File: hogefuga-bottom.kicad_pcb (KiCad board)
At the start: 2 copper layers, 95.2 x 97.6 mm, 6 parts

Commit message: rev0.2
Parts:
- removed the REF** at (90.5, 126.2)
- removed the REF** at (147.6, 88.1)
- removed the REF** at (90.5, 88.1)
- removed the REF** at (147.6, 126.2)
- added REF**: MountingHole_2.2mm_M2, MountingHole:MountingHole_2.2mm_M2, F.Cu at (131.0, 78.6)
- added REF**: MountingHole_2.2mm_M2, MountingHole:MountingHole_2.2mm_M2, F.Cu at (131.0, 116.7)
- added REF**: MountingHole_2.2mm_M2, MountingHole:MountingHole_2.2mm_M2, F.Cu at (73.8, 116.7)
- added REF**: MountingHole_2.2mm_M2, MountingHole:MountingHole_2.2mm_M2, F.Cu at (73.8, 78.6)
- moved G*** 19.2 mm to (102.4, 100.0) (x2)
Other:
- board size 95.2 x 97.6 mm -> 95.3 x 97.6 mm

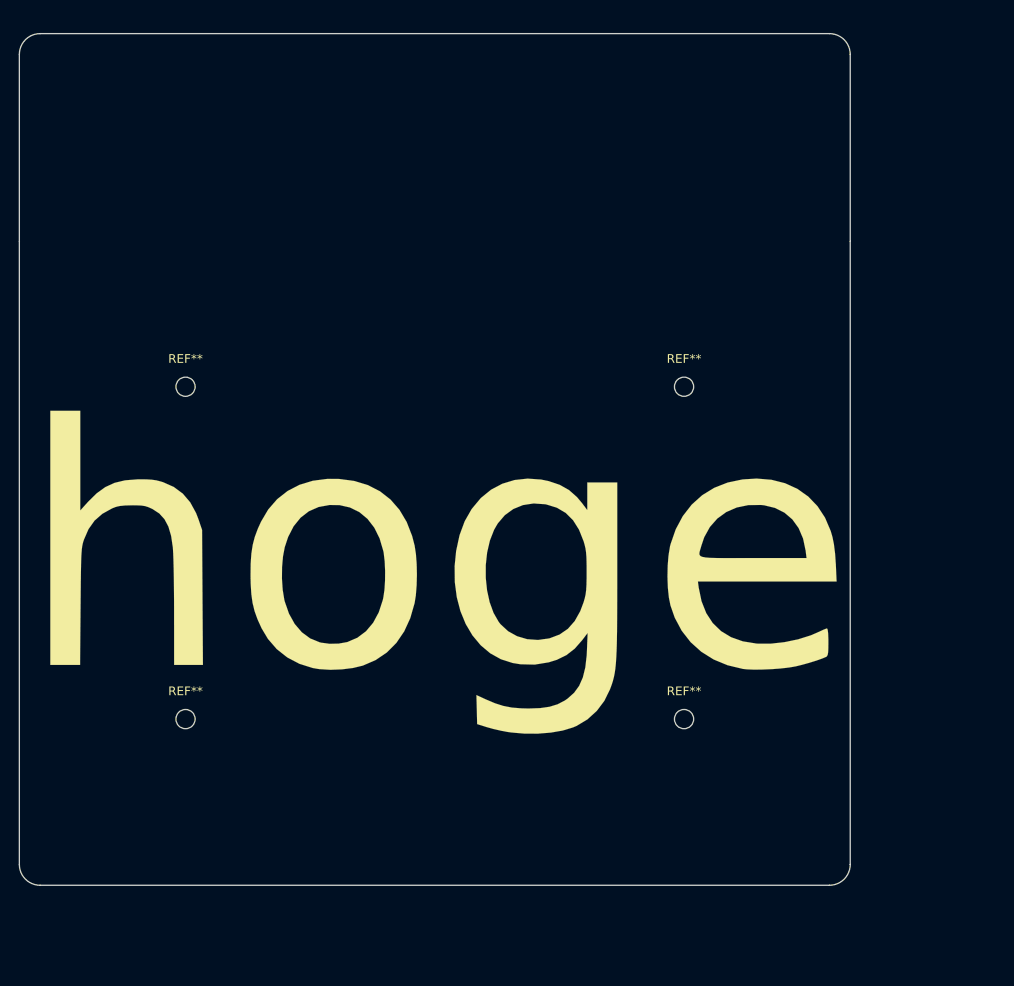
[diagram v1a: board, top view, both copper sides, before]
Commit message: PCBを直接ボトムプレートに固定する穴を追加
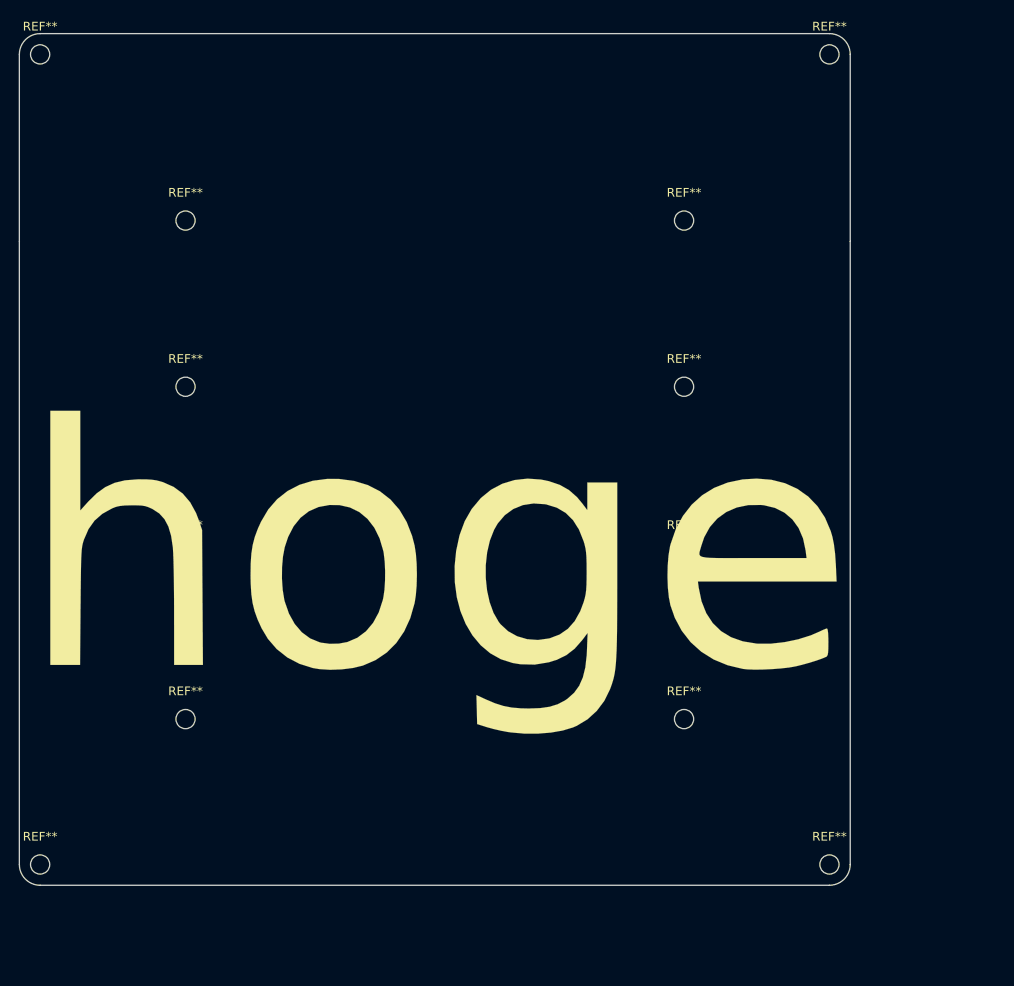
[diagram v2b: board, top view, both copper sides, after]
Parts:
- added REF**: MountingHole_2.2mm_M2, MountingHole:MountingHole_2.2mm_M2, F.Cu at (73.8, 97.6)
- added REF**: MountingHole_2.2mm_M2, MountingHole:MountingHole_2.2mm_M2, F.Cu at (73.8, 59.5)
- added REF**: MountingHole_2.2mm_M2, MountingHole:MountingHole_2.2mm_M2, F.Cu at (131.0, 59.5)
- added REF**: MountingHole_2.2mm_M2, MountingHole:MountingHole_2.2mm_M2, F.Cu at (147.6, 40.5)
- added REF**: MountingHole_2.2mm_M2, MountingHole:MountingHole_2.2mm_M2, F.Cu at (57.1, 40.5)
- added REF**: MountingHole_2.2mm_M2, MountingHole:MountingHole_2.2mm_M2, F.Cu at (57.1, 133.3)
- added REF**: MountingHole_2.2mm_M2, MountingHole:MountingHole_2.2mm_M2, F.Cu at (147.6, 133.3)
- added REF**: MountingHole_2.2mm_M2, MountingHole:MountingHole_2.2mm_M2, F.Cu at (131.0, 97.6)
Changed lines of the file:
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@@
     (tracks 0)
     (zones 0)
-    (modules 6)
+    (modules 14)
     (nets 1)
   )
@@
     (34 B.Paste user)
     (35 F.Paste user)
-    (36 B.SilkS user)
-    (37 F.SilkS user)
+    (36 B.SilkS user hide)
+    (37 F.SilkS user hide)
     (38 B.Mask user)
     (39 F.Mask user)
@@
       (xy 4.326291 11.84335) (xy 5.83656 12.123249) (xy 7.203423 12.18999) (xy 8.924412 12.091771)) (layer B.SilkS) (width 0.01))
   )
+  (module MountingHole:MountingHole_2.2mm_M2 (layer F.Cu)
+    (at 147.6375 40.48125)
+    (descr "Mounting Hole 2.2mm, no annular, M2")
+    (tags "mounting hole 2.2mm no annular m2")
+    (attr virtual)
+    (fp_text reference REF** (at 0 -3.2) (layer F.SilkS)
+      (effects (font (size 1 1) (thickness 0.15)))
+    )
+    (fp_text value MountingHole_2.2mm_M2 (at 0 3.2) (layer F.Fab)
+      (effects (font (size 1 1) (thickness 0.15)))
+    )
+    (fp_circle (center 0 0) (end 2.45 0) (layer F.CrtYd) (width 0.05))
+    (fp_circle (center 0 0) (end 2.2 0) (layer Cmts.User) (width 0.15))
+    (fp_text user %R (at 0.3 0) (layer F.Fab)
+      (effects (font (size 1 1) (thickness 0.15)))
+    )
+    (pad 1 np_thru_hole circle (at 0 0) (size 2.2 2.2) (drill 2.2) (layers *.Cu *.Mask))
+  )
+  (module MountingHole:MountingHole_2.2mm_M2 (layer F.Cu)
+    (at 57.15 40.48125)
+    (descr "Mounting Hole 2.2mm, no annular, M2")
+    (tags "mounting hole 2.2mm no annular m2")
+    (attr virtual)
+    (fp_text reference REF** (at 0 -3.2) (layer F.SilkS)
+      (effects (font (size 1 1) (thickness 0.15)))
+    )
+    (fp_text value MountingHole_2.2mm_M2 (at 0 3.2) (layer F.Fab)
+      (effects (font (size 1 1) (thickness 0.15)))
+    )
+    (fp_circle (center 0 0) (end 2.45 0) (layer F.CrtYd) (width 0.05))
+    (fp_circle (center 0 0) (end 2.2 0) (layer Cmts.User) (width 0.15))
+    (fp_text user %R (at 0.3 0) (layer F.Fab)
+      (effects (font (size 1 1) (thickness 0.15)))
+    )
+    (pad 1 np_thru_hole circle (at 0 0) (size 2.2 2.2) (drill 2.2) (layers *.Cu *.Mask))
+  )
+  (module MountingHole:MountingHole_2.2mm_M2 (layer F.Cu)
+    (at 57.15 133.35)
+    (descr "Mounting Hole 2.2mm, no annular, M2")
+    (tags "mounting hole 2.2mm no annular m2")
+    (attr virtual)
+    (fp_text reference REF** (at 0 -3.2) (layer F.SilkS)
+      (effects (font (size 1 1) (thickness 0.15)))
+    )
+    (fp_text value MountingHole_2.2mm_M2 (at 0 3.2) (layer F.Fab)
+      (effects (font (size 1 1) (thickness 0.15)))
+    )
+    (fp_circle (center 0 0) (end 2.45 0) (layer F.CrtYd) (width 0.05))
+    (fp_circle (center 0 0) (end 2.2 0) (layer Cmts.User) (width 0.15))
+    (fp_text user %R (at 0.3 0) (layer F.Fab)
+      (effects (font (size 1 1) (thickness 0.15)))
+    )
+    (pad 1 np_thru_hole circle (at 0 0) (size 2.2 2.2) (drill 2.2) (layers *.Cu *.Mask))
+  )
+  (module MountingHole:MountingHole_2.2mm_M2 (layer F.Cu)
+    (at 147.6375 133.35)
+    (descr "Mounting Hole 2.2mm, no annular, M2")
+    (tags "mounting hole 2.2mm no annular m2")
+    (attr virtual)
+    (fp_text reference REF** (at 0 -3.2) (layer F.SilkS)
+      (effects (font (size 1 1) (thickness 0.15)))
+    )
+    (fp_text value MountingHole_2.2mm_M2 (at 0 3.2) (layer F.Fab)
+      (effects (font (size 1 1) (thickness 0.15)))
+    )
+    (fp_circle (center 0 0) (end 2.45 0) (layer F.CrtYd) (width 0.05))
+    (fp_circle (center 0 0) (end 2.2 0) (layer Cmts.User) (width 0.15))
+    (fp_text user %R (at 0.3 0) (layer F.Fab)
+      (effects (font (size 1 1) (thickness 0.15)))
+    )
+    (pad 1 np_thru_hole circle (at 0 0) (size 2.2 2.2) (drill 2.2) (layers *.Cu *.Mask))
+  )
+  (module MountingHole:MountingHole_2.2mm_M2 (layer F.Cu)
+    (at 130.96875 97.63125)
+    (descr "Mounting Hole 2.2mm, no annular, M2")
+    (tags "mounting hole 2.2mm no annular m2")
+    (attr virtual)
+    (fp_text reference REF** (at 0 -3.2) (layer F.SilkS)
+      (effects (font (size 1 1) (thickness 0.15)))
+    )
+    (fp_text value MountingHole_2.2mm_M2 (at 0 3.2) (layer F.Fab)
+      (effects (font (size 1 1) (thickness 0.15)))
+    )
+    (fp_circle (center 0 0) (end 2.45 0) (layer F.CrtYd) (width 0.05))
+    (fp_circle (center 0 0) (end 2.2 0) (layer Cmts.User) (width 0.15))
+    (fp_text user %R (at 0.3 0) (layer F.Fab)
+      (effects (font (size 1 1) (thickness 0.15)))
+    )
+    (pad 1 np_thru_hole circle (at 0 0) (size 2.2 2.2) (drill 2.2) (layers *.Cu *.Mask))
+  )
+  (module MountingHole:MountingHole_2.2mm_M2 (layer F.Cu)
+    (at 73.81875 97.63125)
+    (descr "Mounting Hole 2.2mm, no annular, M2")
+    (tags "mounting hole 2.2mm no annular m2")
+    (attr virtual)
+    (fp_text reference REF** (at 0 -3.2) (layer F.SilkS)
+      (effects (font (size 1 1) (thickness 0.15)))
+    )
+    (fp_text value MountingHole_2.2mm_M2 (at 0 3.2) (layer F.Fab)
+      (effects (font (size 1 1) (thickness 0.15)))
+    )
+    (fp_circle (center 0 0) (end 2.45 0) (layer F.CrtYd) (width 0.05))
+    (fp_circle (center 0 0) (end 2.2 0) (layer Cmts.User) (width 0.15))
+    (fp_text user %R (at 0.3 0) (layer F.Fab)
+      (effects (font (size 1 1) (thickness 0.15)))
+    )
+    (pad 1 np_thru_hole circle (at 0 0) (size 2.2 2.2) (drill 2.2) (layers *.Cu *.Mask))
+  )
+  (module MountingHole:MountingHole_2.2mm_M2 (layer F.Cu)
+    (at 73.81875 59.53125)
+    (descr "Mounting Hole 2.2mm, no annular, M2")
+    (tags "mounting hole 2.2mm no annular m2")
+    (attr virtual)
+    (fp_text reference REF** (at 0 -3.2) (layer F.SilkS)
+      (effects (font (size 1 1) (thickness 0.15)))
+    )
+    (fp_text value MountingHole_2.2mm_M2 (at 0 3.2) (layer F.Fab)
+      (effects (font (size 1 1) (thickness 0.15)))
+    )
+    (fp_circle (center 0 0) (end 2.45 0) (layer F.CrtYd) (width 0.05))
+    (fp_circle (center 0 0) (end 2.2 0) (layer Cmts.User) (width 0.15))
+    (fp_text user %R (at 0.3 0) (layer F.Fab)
+      (effects (font (size 1 1) (thickness 0.15)))
+    )
+    (pad 1 np_thru_hole circle (at 0 0) (size 2.2 2.2) (drill 2.2) (layers *.Cu *.Mask))
+  )
+  (module MountingHole:MountingHole_2.2mm_M2 (layer F.Cu)
+    (at 130.96875 59.53125)
+    (descr "Mounting Hole 2.2mm, no annular, M2")
+    (tags "mounting hole 2.2mm no annular m2")
+    (attr virtual)
+    (fp_text reference REF** (at 0 -3.2) (layer F.SilkS)
+      (effects (font (size 1 1) (thickness 0.15)))
+    )
+    (fp_text value MountingHole_2.2mm_M2 (at 0 3.2) (layer F.Fab)
+      (effects (font (size 1 1) (thickness 0.15)))
+    )
+    (fp_circle (center 0 0) (end 2.45 0) (layer F.CrtYd) (width 0.05))
+    (fp_circle (center 0 0) (end 2.2 0) (layer Cmts.User) (width 0.15))
+    (fp_text user %R (at 0.3 0) (layer F.Fab)
+      (effects (font (size 1 1) (thickness 0.15)))
+    )
+    (pad 1 np_thru_hole circle (at 0 0) (size 2.2 2.2) (drill 2.2) (layers *.Cu *.Mask))
+  )
   (gr_line (start 150.01875 61.9125) (end 150.01875 40.48125) (layer Edge.Cuts) (width 0.15))

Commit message: ボトムプレートの片面を導体で塗りつぶす試み
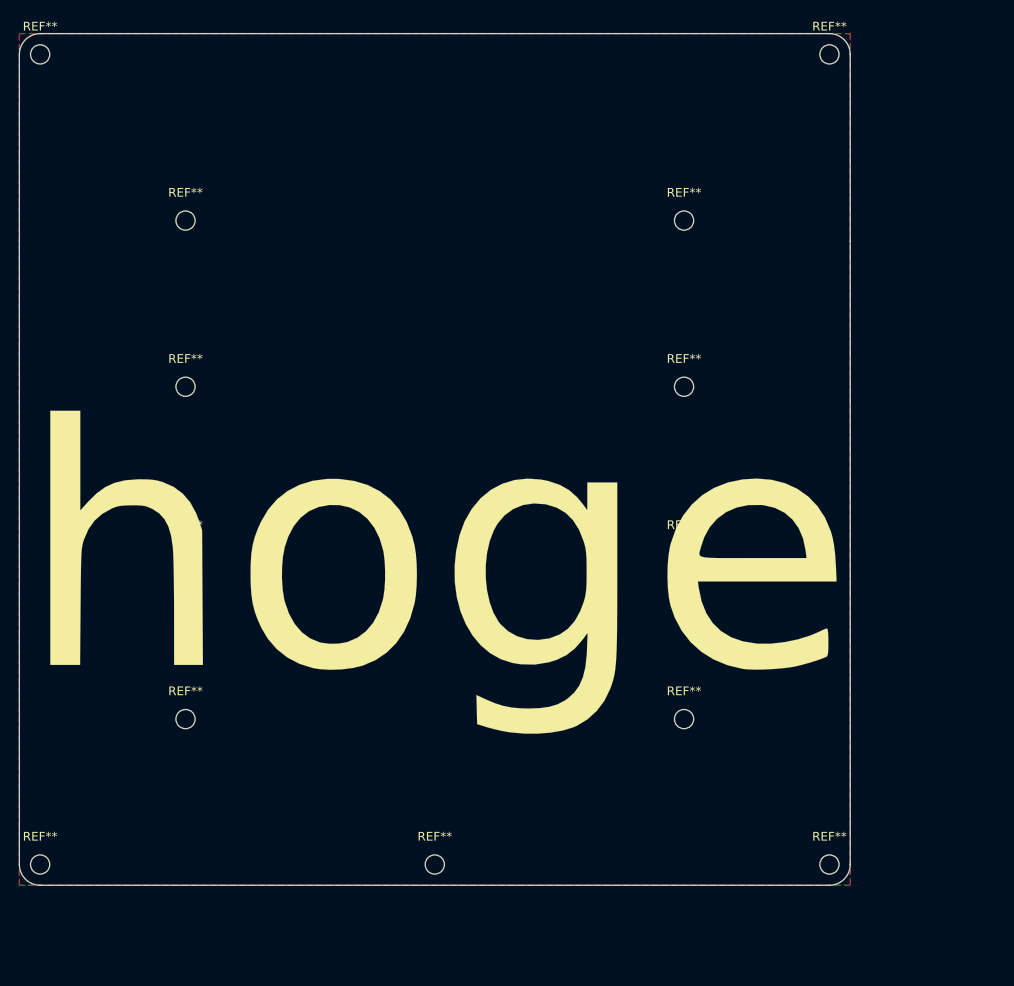
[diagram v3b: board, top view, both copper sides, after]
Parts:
- added REF**: MountingHole_2.2mm_M2, MountingHole:MountingHole_2.2mm_M2, F.Cu at (102.4, 133.3)
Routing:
- added copper zone on F.Cu, net (none)
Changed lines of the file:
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@@
     (tracks 0)
     (zones 0)
-    (modules 14)
+    (modules 15)
     (nets 1)
   )
@@
     (34 B.Paste user)
     (35 F.Paste user)
-    (36 B.SilkS user hide)
-    (37 F.SilkS user hide)
+    (36 B.SilkS user)
+    (37 F.SilkS user)
     (38 B.Mask user)
     (39 F.Mask user)
@@
       (drillshape 0)
       (scaleselection 1)
-      (outputdirectory "garber/pcb/"))
+      (outputdirectory "garber/bottom/"))
   )
   (net 0 "")
@@
     (pad 1 np_thru_hole circle (at 0 0) (size 2.2 2.2) (drill 2.2) (layers *.Cu *.Mask))
   )
+  (module MountingHole:MountingHole_2.2mm_M2 (layer F.Cu)
+    (at 102.39375 133.35)
+    (descr "Mounting Hole 2.2mm, no annular, M2")
+    (tags "mounting hole 2.2mm no annular m2")
+    (attr virtual)
+    (fp_text reference REF** (at 0 -3.2) (layer F.SilkS)
+      (effects (font (size 1 1) (thickness 0.15)))
+    )
+    (fp_text value MountingHole_2.2mm_M2 (at 0 3.2) (layer F.Fab)
+      (effects (font (size 1 1) (thickness 0.15)))
+    )
+    (fp_circle (center 0 0) (end 2.45 0) (layer F.CrtYd) (width 0.05))
+    (fp_circle (center 0 0) (end 2.2 0) (layer Cmts.User) (width 0.15))
+    (fp_text user %R (at 0.3 0) (layer F.Fab)
+      (effects (font (size 1 1) (thickness 0.15)))
+    )
+    (pad 1 np_thru_hole circle (at 0 0) (size 2.2 2.2) (drill 2.2) (layers *.Cu *.Mask))
+  )
   (gr_line (start 150.01875 61.9125) (end 150.01875 40.48125) (layer Edge.Cuts) (width 0.15))
   (gr_line (start 54.76875 61.9125) (end 54.76875 40.48125) (layer Edge.Cuts) (width 0.15))
@@
     (arrow2b (pts (xy 161.925 135.73125) (xy 161.338579 134.604746)))
   )
+  (zone (net 0) (net_name "") (layer F.Cu) (hatch edge 0.508)
+    (connect_pads (clearance 0.508))
+    (min_thickness 0.254)
+    (fill yes (arc_segments 16) (thermal_gap 0.508) (thermal_bridge_width 0.508) (smoothing fillet) (radius 1))
+    (polygon
+      (pts
+        (xy 150.01875 38.1) (xy 150.01875 135.73125) (xy 54.76875 135.73125) (xy 54.76875 38.1)
+      )
+    )
+  )
 )

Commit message: プレートからボトムへのネジを追加
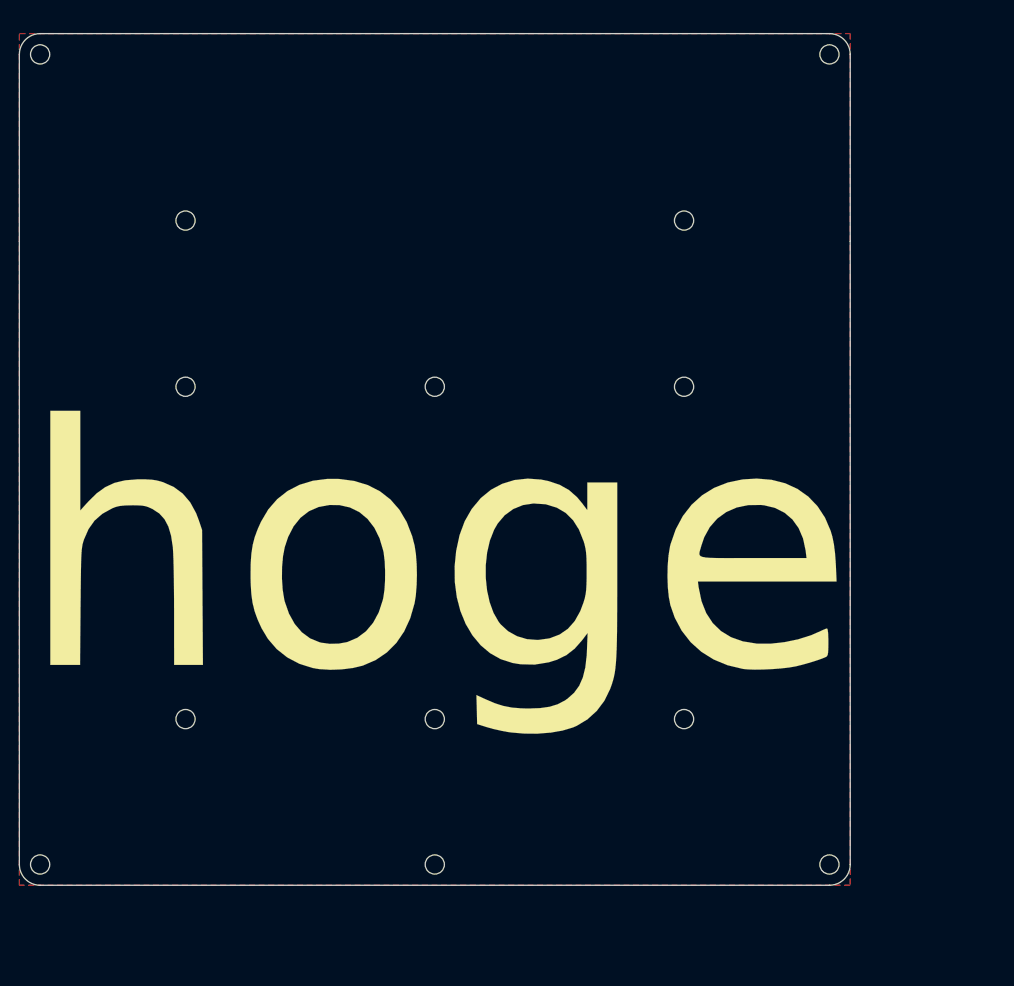
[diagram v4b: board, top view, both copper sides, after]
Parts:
- removed REF** (x13): MountingHole_2.2mm_M2, MountingHole:MountingHole_2.2mm_M2
- added ?: M2, lib:MountingHole_2.2mm_M2, F.Cu at (147.6, 40.5)
- added ?: M2, lib:MountingHole_2.2mm_M2, F.Cu at (73.8, 97.6)
- added ?: M2, lib:MountingHole_2.2mm_M2, F.Cu at (73.8, 78.6)
- added ?: M2, lib:MountingHole_2.2mm_M2, F.Cu at (73.8, 59.5)
- added ?: M2, lib:MountingHole_2.2mm_M2, F.Cu at (57.1, 40.5)
- added ?: M2, lib:MountingHole_2.2mm_M2, F.Cu at (102.4, 78.6)
- added ?: M2, lib:MountingHole_2.2mm_M2, F.Cu at (102.4, 116.7)
- added ?: M2, lib:MountingHole_2.2mm_M2, F.Cu at (131.0, 59.5)
- added ?: M2, lib:MountingHole_2.2mm_M2, F.Cu at (131.0, 78.6)
- added ?: M2, lib:MountingHole_2.2mm_M2, F.Cu at (131.0, 97.6)
- added ?: M2, lib:MountingHole_2.2mm_M2, F.Cu at (131.0, 116.7)
- added ?: M2, lib:MountingHole_2.2mm_M2, F.Cu at (147.6, 133.3)
- added ?: M2, lib:MountingHole_2.2mm_M2, F.Cu at (102.4, 133.3)
- added ?: M2, lib:MountingHole_2.2mm_M2, F.Cu at (57.1, 133.3)
- added ?: M2, lib:MountingHole_2.2mm_M2, F.Cu at (73.8, 116.7)
